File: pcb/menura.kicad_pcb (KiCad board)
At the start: 2 copper layers, 123 x 97.2 mm, 55 parts, among them SW1 SW_Push, SW10 SW_Push, SW11 SW_Push, SW12 SW_Push, SW13 SW_Push, SW14 SW_Push, SW15 SW_Push, SW16 SW_Push, SW17 SW_Push, SW18 SW_Push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

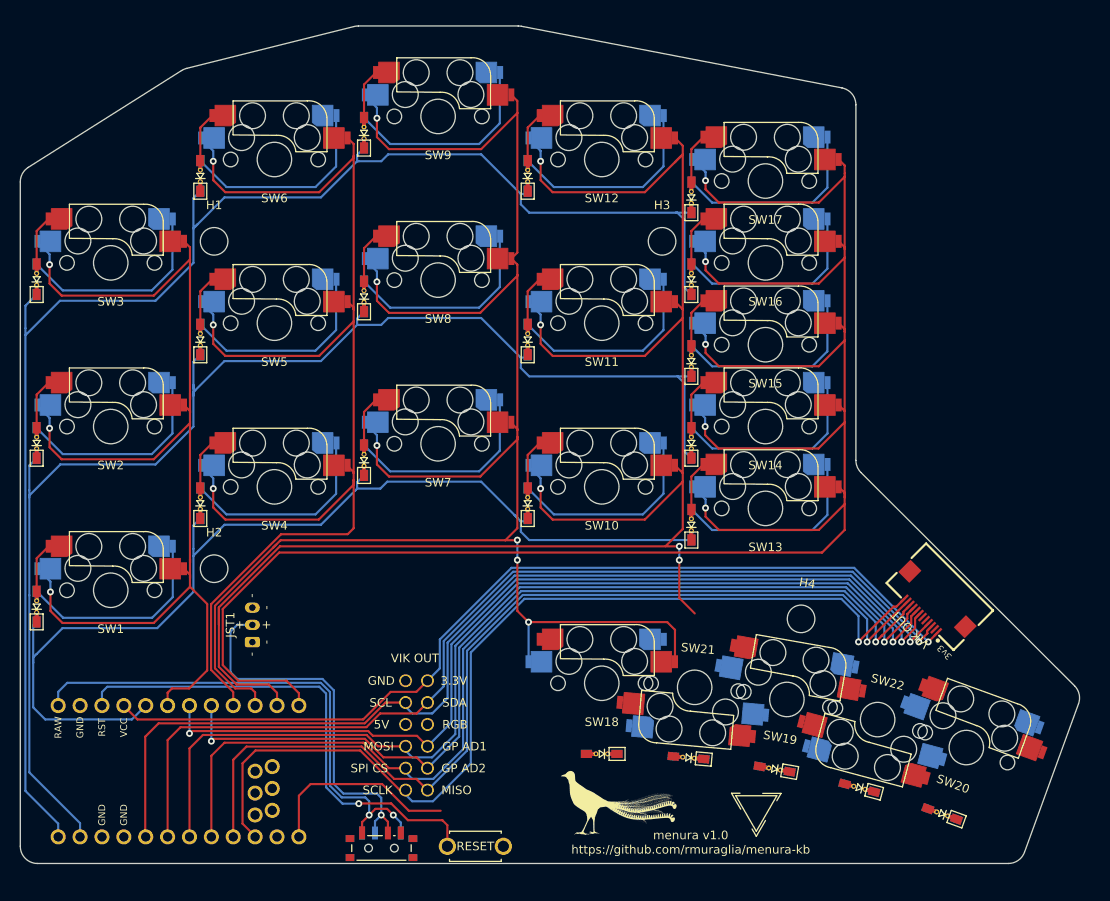
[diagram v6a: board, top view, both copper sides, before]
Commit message: rough cols 2 and 4
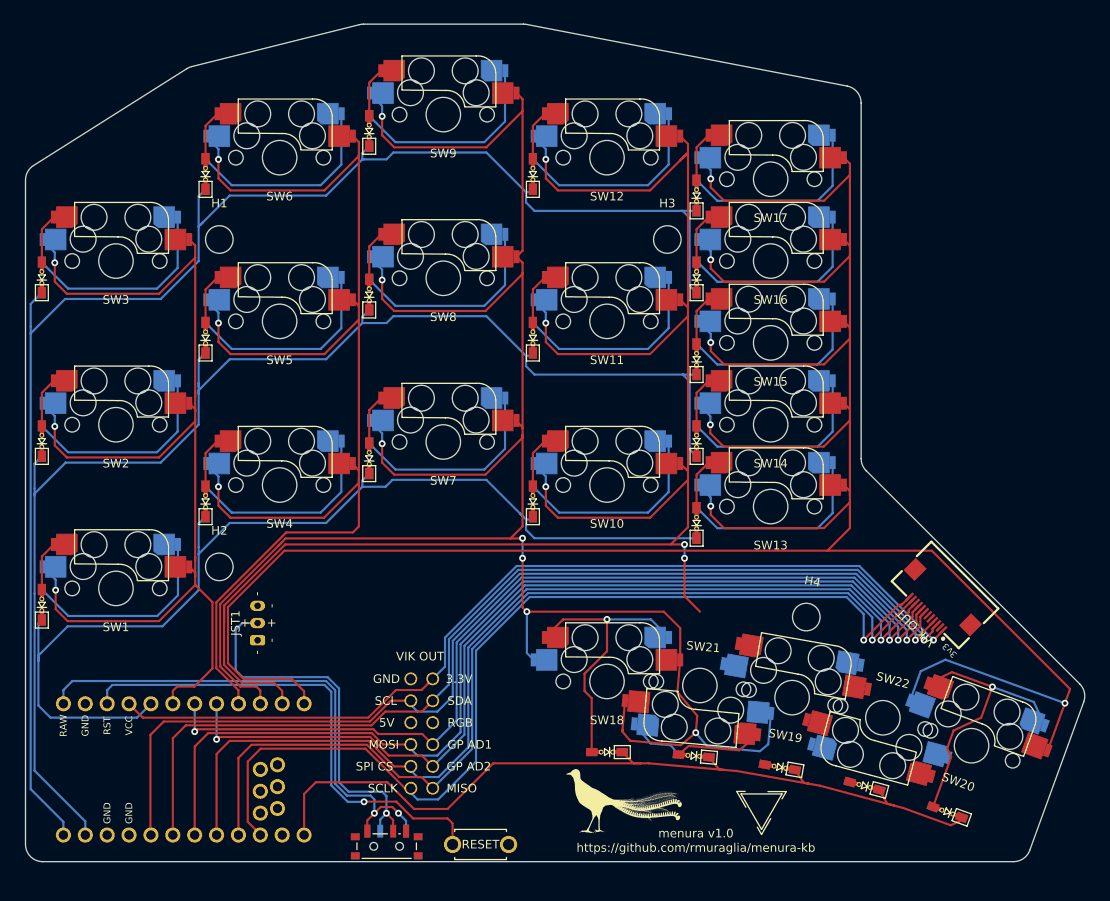
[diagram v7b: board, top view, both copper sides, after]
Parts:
- moved D12 0.64 mm to (149.0, 51.7)
- moved H3 0.64 mm to (164.6, 59.3)
- moved SW6 0.64 mm to (119.6, 49.8)
- moved H2 0.64 mm to (112.6, 97.3)
- moved D21 0.64 mm to (167.7, 119.2)
- moved SW13 0.64 mm to (176.6, 90.3)
- moved D4 0.64 mm to (111.0, 89.7)
- moved D5 0.64 mm to (111.0, 70.7)
- moved SW4 0.64 mm to (119.6, 87.8)
- moved D10 0.64 mm to (149.0, 89.7)
- moved D17 0.64 mm to (168.0, 54.2)
- moved MCU1 0.64 mm to (107.6, 120.4)
- moved SW16 0.64 mm to (176.6, 61.8)
- moved SW21 0.64 mm to (168.4, 111.1)
- moved SW8 0.64 mm to (138.6, 63.8)
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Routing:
- net row3: track 23.1 -> 96.5 mm
- net col4: track 253.3 -> 317.2 mm, vias 5 -> 6
- net col2: track 216.3 -> 253.1 mm, vias 6 -> 7
- net Net-(D20-A): track 0.00 -> 33.0 mm, vias 0 -> 1
- net Net-(D18-A): track 0.00 -> 33.0 mm, vias 0 -> 1
- net Net-(D21-A): track 0.00 -> 17.0 mm

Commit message: thumbs sloppy but done
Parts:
- moved D14 1.12 mm to (168.9, 82.0)
- moved MCU1 1.12 mm to (108.5, 119.7)
- moved D10 1.12 mm to (149.9, 89.0)
- moved H3 1.12 mm to (165.5, 58.6)
- moved D17 1.12 mm to (168.9, 53.5)
- moved D6 1.12 mm to (111.9, 51.0)
- moved H1 1.12 mm to (113.5, 58.6)
- moved D7 1.12 mm to (130.9, 84.0)
- moved SW3 1.12 mm to (101.5, 61.1)
- moved SW21 1.12 mm to (169.2, 110.3)
- moved D8 1.12 mm to (130.9, 65.0)
- moved SW2 1.12 mm to (101.5, 80.1)
- moved SW4 1.12 mm to (120.5, 87.1)
- moved SW7 1.12 mm to (139.5, 82.1)
- moved D2 1.12 mm to (92.9, 82.0)
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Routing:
- net col3: track 208.7 -> 273.2 mm, vias 5 -> 7
- net Net-(D19-A): track 0.00 -> 32.3 mm, vias 0 -> 1
- net Net-(D22-A): track 0.00 -> 17.0 mm
- net col4: track 317.2 -> 316.2 mm
